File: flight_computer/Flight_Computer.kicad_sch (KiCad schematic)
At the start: 115 parts

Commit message: name
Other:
- note added: "Baker Wong"
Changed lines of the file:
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@@
+    (effects (font (size 1.27 1.27)) (justify left bottom))
+  )
+  (text "Baker Wong" (at 312.42 175.26 0)
     (effects (font (size 1.27 1.27)) (justify left bottom))
   )

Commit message: GNBD
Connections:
- net GND: now also J?.3 (Pin_3)
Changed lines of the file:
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@@
+    (pin "1")
+  )
+  (symbol (lib_id "power:GND") (at 119.38 153.67 90) (unit 1)
+    (in_bom yes) (on_board yes) (fields_autoplaced)
+    (property "Reference" "#PWR?" (id 0) (at 125.73 153.67 0)
+      (effects (font (size 1.27 1.27)) hide)
+    )
+    (property "Value" "GND" (id 1) (at 123.19 153.6699 90)
+      (effects (font (size 1.27 1.27)) (justify right))
+    )
+    (property "Footprint" "" (id 2) (at 119.38 153.67 0)
+      (effects (font (size 1.27 1.27)) hide)
+    )
+    (property "Datasheet" "" (id 3) (at 119.38 153.67 0)
+      (effects (font (size 1.27 1.27)) hide)
+    )
     (pin "1")
   )
@@
       (reference "#PWR?") (unit 1) (value "GND") (footprint "")
     )
+    (path "/57535ee3-b0ed-45a3-b245-48c5e387c69d"
+      (reference "#PWR?") (unit 1) (value "GND") (footprint "")
+    )

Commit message: conn
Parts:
- added J?: Conn_01x02_Male, symbol Connector:Conn_01x02_Male
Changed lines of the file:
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@@
     (pin "1")
   )
+  (symbol (lib_id "Connector:Conn_01x02_Male") (at 134.62 143.51 0) (unit 1)
+    (in_bom yes) (on_board yes) (fields_autoplaced)
+    (property "Reference" "J?" (id 0) (at 135.255 138.43 0))
+    (property "Value" "Conn_01x02_Male" (id 1) (at 135.255 140.97 0))
+    (property "Footprint" "" (id 2) (at 134.62 143.51 0)
+      (effects (font (size 1.27 1.27)) hide)
+    )
+    (property "Datasheet" "~" (id 3) (at 134.62 143.51 0)
+      (effects (font (size 1.27 1.27)) hide)
+    )
+    (pin "1")
+    (pin "2")
+  )
   (symbol (lib_id "Device:C") (at 400.05 68.58 270) (unit 1)
     (in_bom yes) (on_board yes)
@@
       (reference "J?") (unit 1) (value ">5V input/ Servo Power") (footprint "")
     )
+    (path "/2875cc79-be52-443d-973a-c115fa048432"
+      (reference "J?") (unit 1) (value "Conn_01x02_Male") (footprint "")
+    )
     (path "/3398c3d3-e0c1-4610-91ed-773d855666d4"

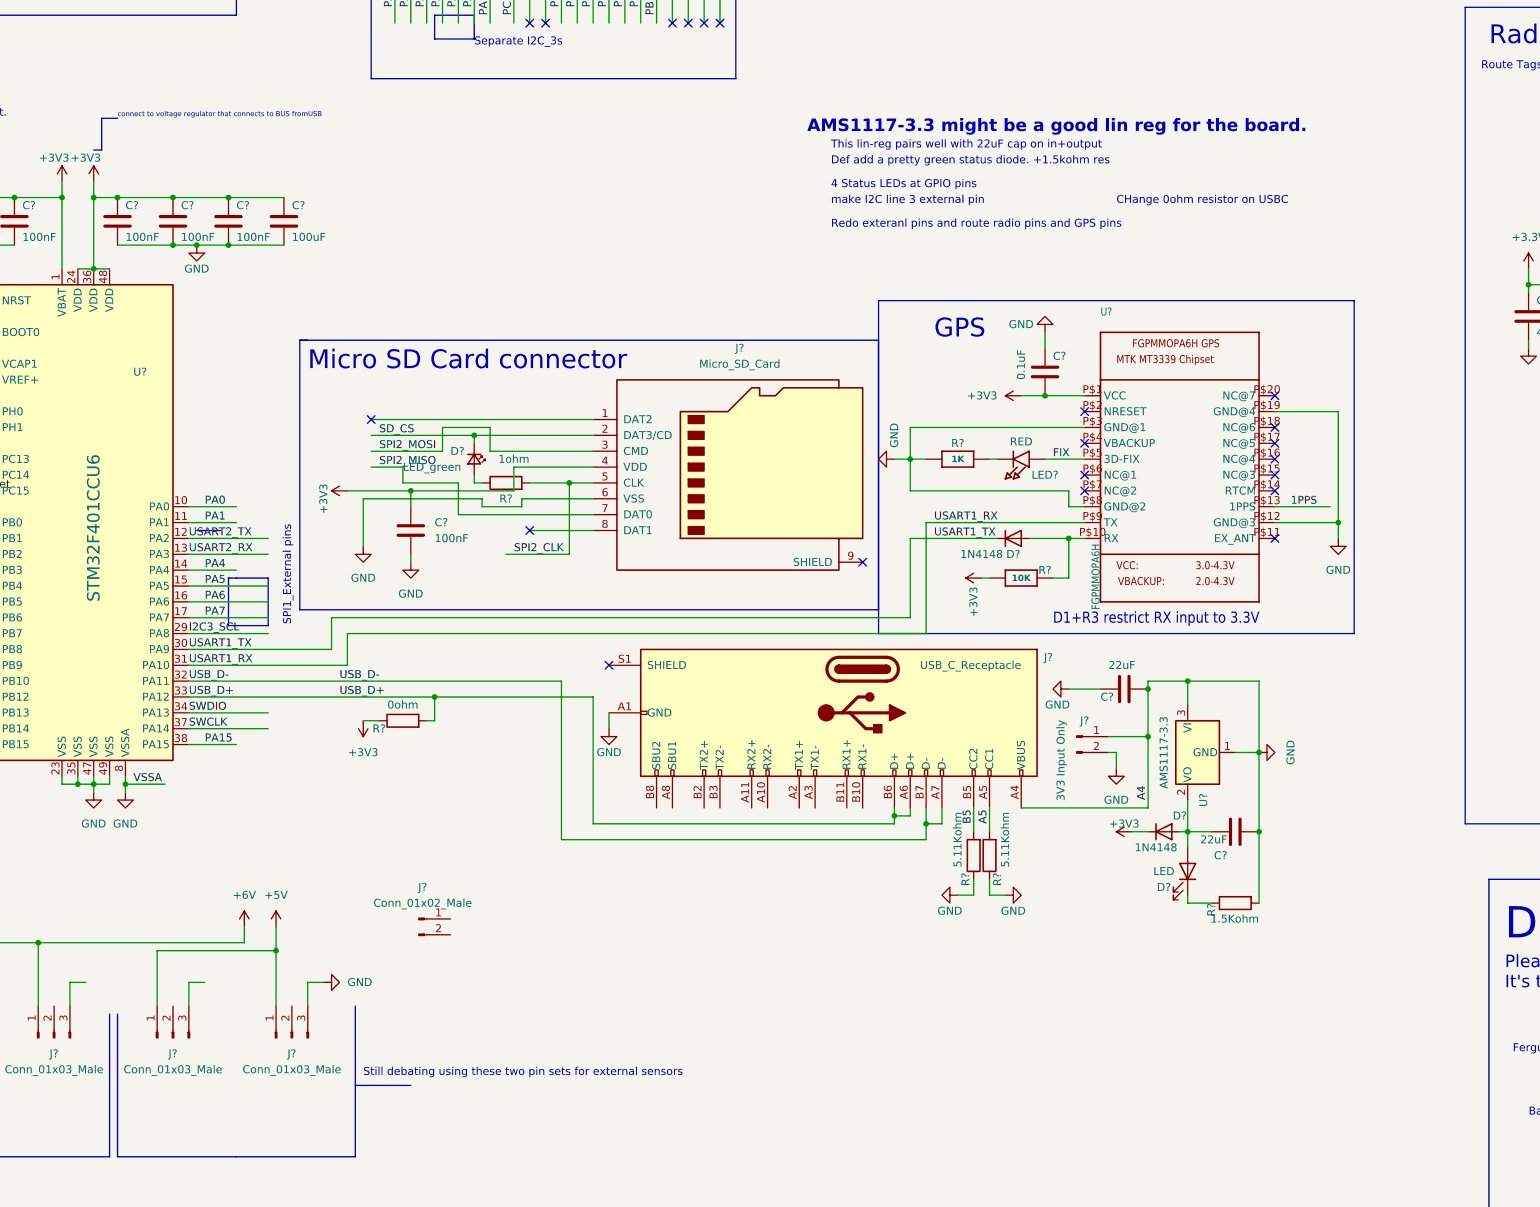
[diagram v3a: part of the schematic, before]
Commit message: DeleteAMS1117
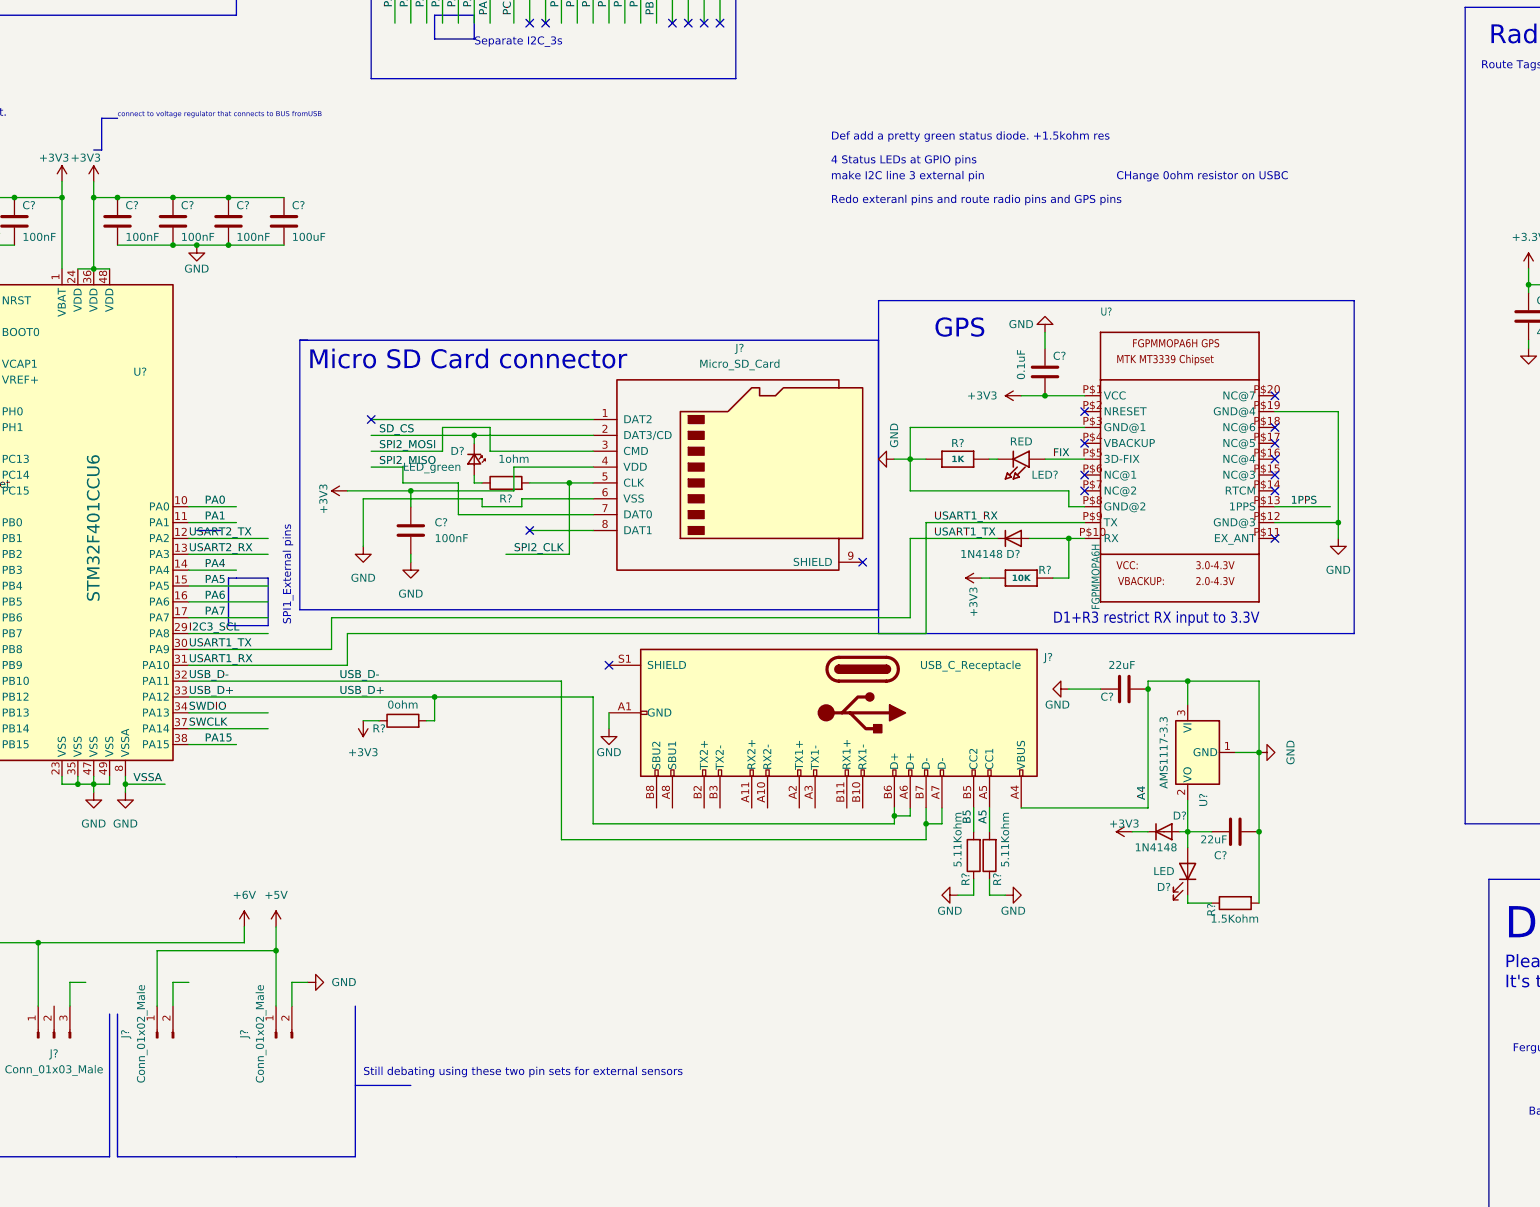
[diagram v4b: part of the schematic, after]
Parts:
- removed J?: 3V3 Input Only, symbol Connector:Conn_01x02_Male
- removed J? (x2): Conn_01x03_Male, symbol Connector:Conn_01x03_Male
- added J?: Conn_01x02_Male, symbol Connector:Conn_01x02_Male
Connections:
- net +5V: now also J?.1 (Pin_1), J?.1 (Pin_1)
- net GND: now also J?.2 (Pin_2)
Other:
- note removed: "AMS1117-3.3 might be a good lin reg for the board."
- note removed: "This lin-reg pairs well with 22uF cap on in+output"
- moved on the sheet: J?

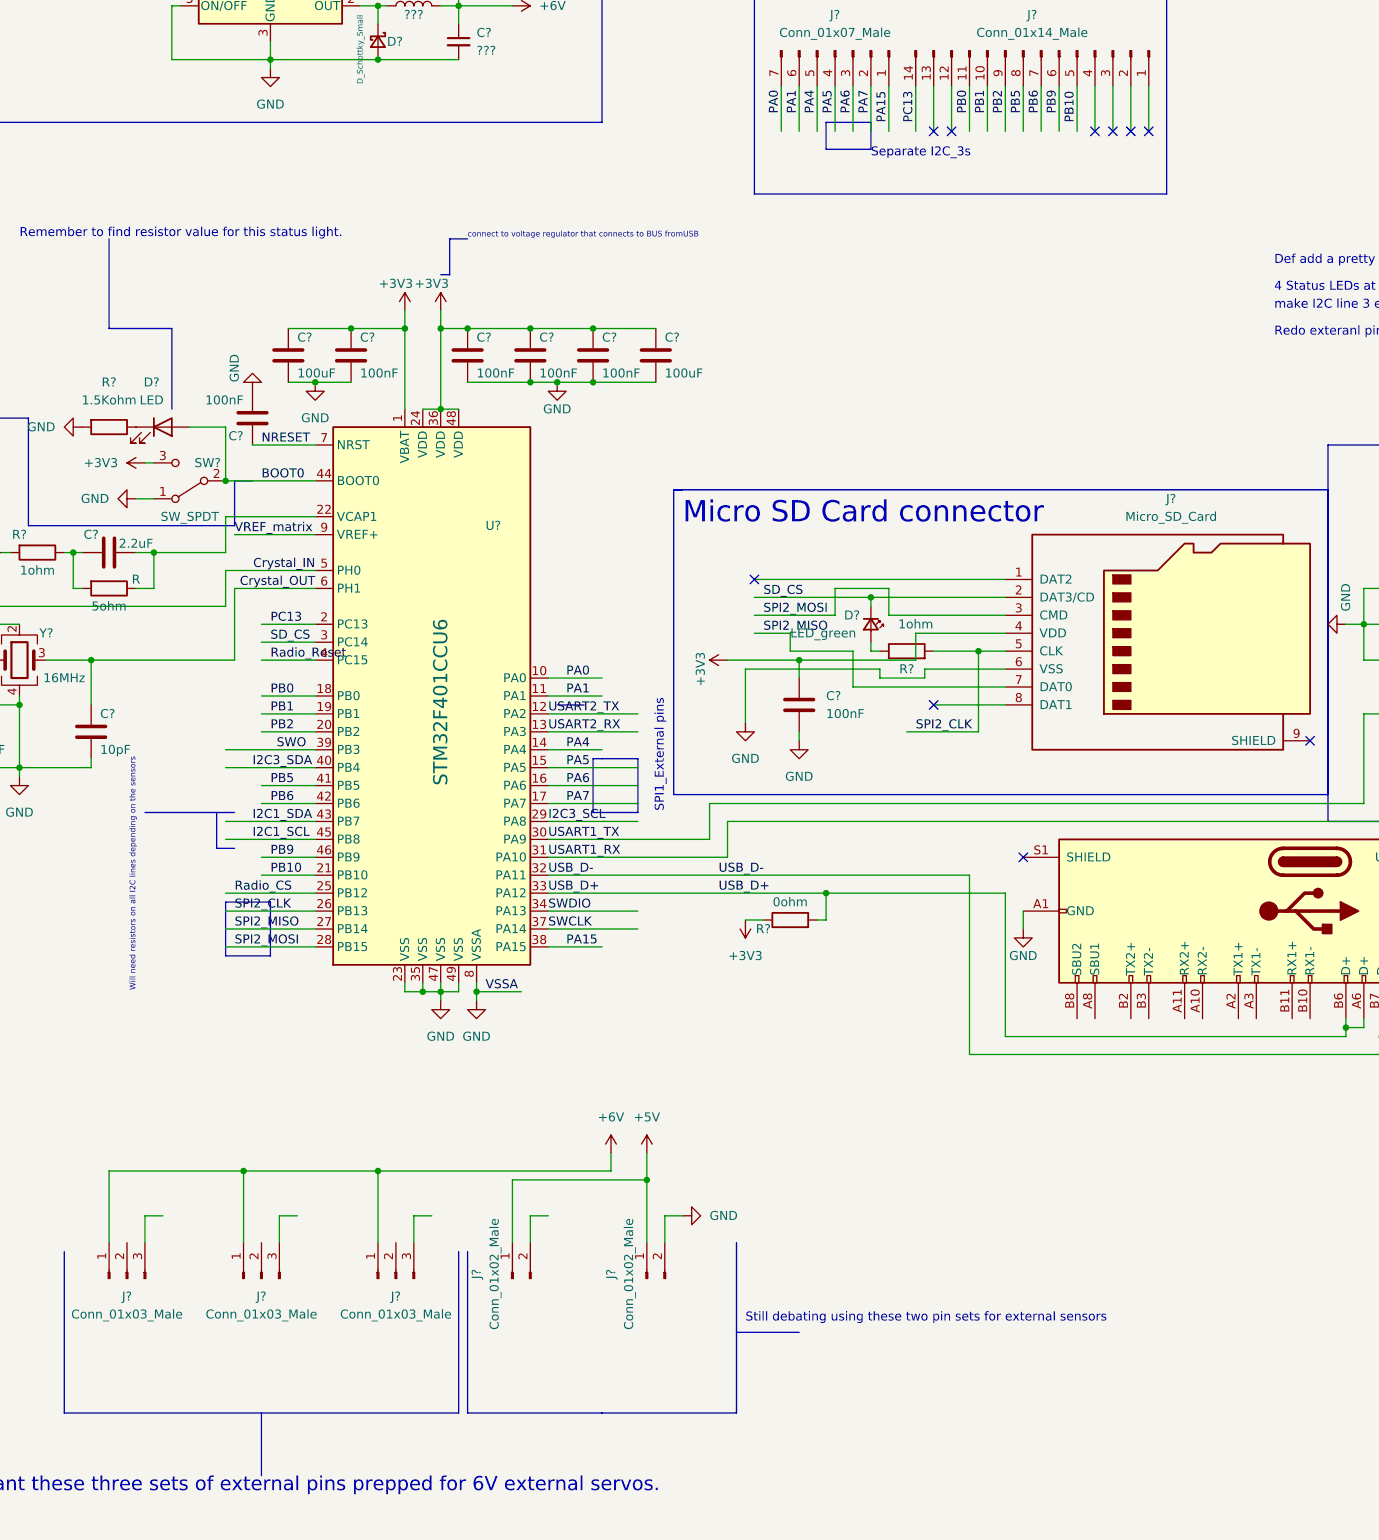
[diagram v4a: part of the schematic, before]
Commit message: I2C lines and Servo pins
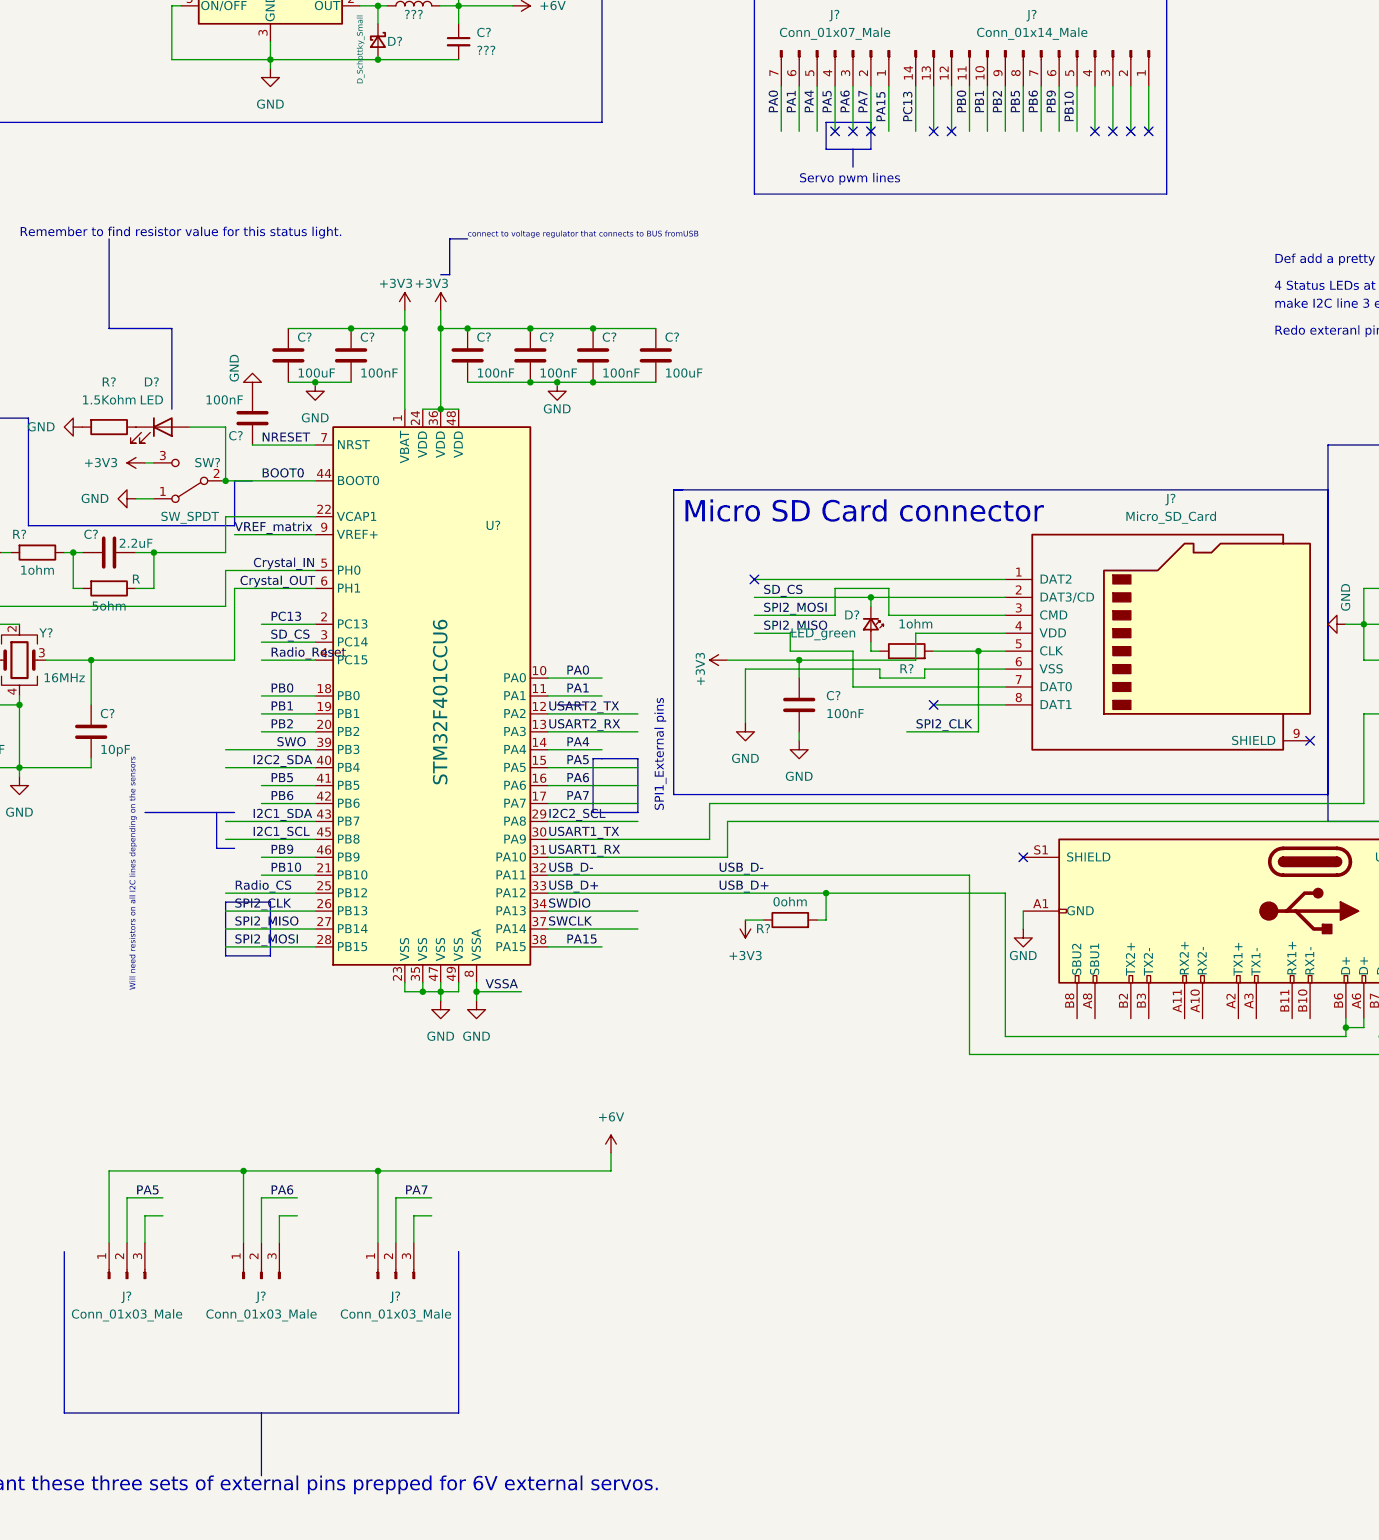
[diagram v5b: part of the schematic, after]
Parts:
- removed J? (x2): Conn_01x02_Male, symbol Connector:Conn_01x02_Male
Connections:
- net I2C3_SCL is gone; now on net I2C2_SCL: U?.29 (PA8)
- net I2C3_SDA is gone; now on net I2C2_SDA: U?.40 (PB4)
- net PA5: now also J?.2 (Pin_2)
- net PA6: now also J?.2 (Pin_2)
- net PA7: now also J?.2 (Pin_2)
- no-connect marks 24 -> 27
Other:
- note added: "Servo pwm lines"
- note removed: "Separate I2C_3s"
- note removed: "Still debating using these two pin sets for external sensors"

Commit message: resistor
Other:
- note added: "3.3 V R1 = 1k R2 = 1.75k"
- note added: "6V R1 = 1k R2 = 4k"
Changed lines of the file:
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@@
+    (stroke (width 0) (type default) (color 0 0 0 0))
+  )
+  (polyline (pts (xy 106.68 -30.48) (xy 124.46 -30.48))
     (stroke (width 0) (type default) (color 0 0 0 0))
   )
@@
     (stroke (width 0) (type default) (color 0 0 0 0))
   )
+  (polyline (pts (xy 106.68 -10.16) (xy 106.68 -30.48))
+    (stroke (width 0) (type default) (color 0 0 0 0))
+  )
   (wire (pts (xy 50.8 274.32) (xy 50.8 276.86))
     (stroke (width 0) (type default) (color 0 0 0 0))
@@
     (stroke (width 0) (type default) (color 0 0 0 0))
   )
+  (polyline (pts (xy 123.19 -10.16) (xy 124.46 -10.16))
+    (stroke (width 0) (type default) (color 0 0 0 0))
+  )
   (wire (pts (xy 143.51 66.04) (xy 162.56 66.04))
     (stroke (width 0) (type default) (color 0 0 0 0))
@@
     (stroke (width 0) (type default) (color 0 0 0 0))
   )
+  (polyline (pts (xy 124.46 -30.48) (xy 124.46 -10.16))
+    (stroke (width 0) (type default) (color 0 0 0 0))
+  )
   (wire (pts (xy 405.13 107.95) (xy 405.13 110.49))
     (stroke (width 0) (type default) (color 0 0 0 0))
@@
   )
   (wire (pts (xy 53.34 57.15) (xy 64.77 57.15))
+    (stroke (width 0) (type default) (color 0 0 0 0))
+  )
+  (polyline (pts (xy 123.19 -10.16) (xy 106.68 -10.16))
     (stroke (width 0) (type default) (color 0 0 0 0))
   )
@@
     (effects (font (size 1.27 1.27) (thickness 0.254) bold italic) (justify left bottom))
   )
+  (text "3.3 V\nR1 = 1k\nR2 = 1.75k" (at 109.22 -22.86 0)
+    (effects (font (size 1.27 1.27)) (justify left bottom))
+  )
   (text "I2C lines 1" (at 6.35 215.9 0)
     (effects (font (size 1.27 1.27)) (justify left bottom))
@@
     (effects (font (size 3 3)) (justify left bottom))
   )
+  (text "6V\nR1 = 1k\nR2 = 4k\n" (at 109.22 -12.7 0)
+    (effects (font (size 1.27 1.27)) (justify left bottom))
+  )
   (text "Route Tags, and route the 3V3" (at 304.8 7.62 0)
